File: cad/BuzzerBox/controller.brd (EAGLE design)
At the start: 100 x 100 mm, 137 parts, among them J2 RASPBERRYPI-40-PIN-GPIO_PTH_N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, Q1 BSS138, Q2 BSS138, Q3 BSS138, T1 BC849, T10 BC849, T2 BC849, T3 BC849, T4 BC849, T5 BC849, T6 BC849, T7 BC849, T8 BC849, T9 BC849, U1 ATMEGA328P-AU, Y1 16MHz

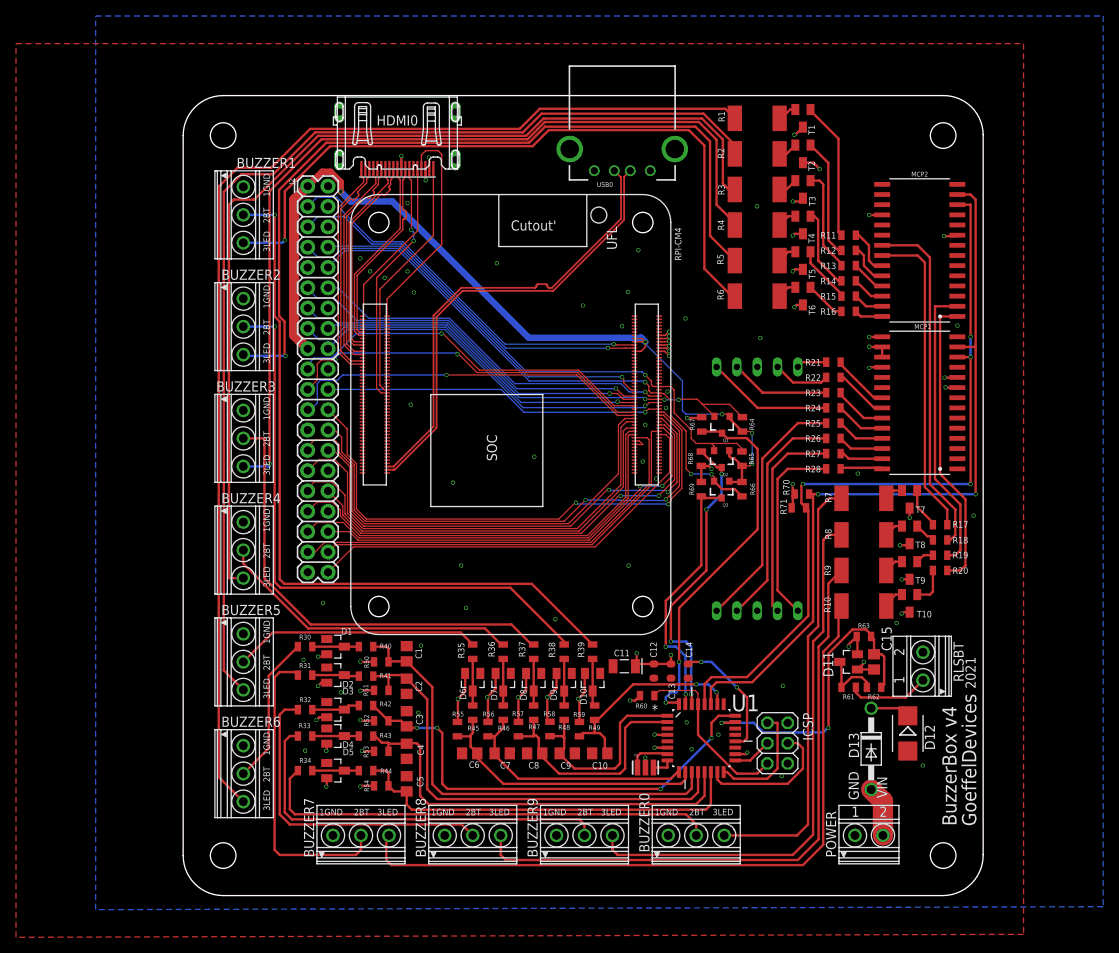
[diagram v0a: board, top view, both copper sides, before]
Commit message: Added combined header for buzzers
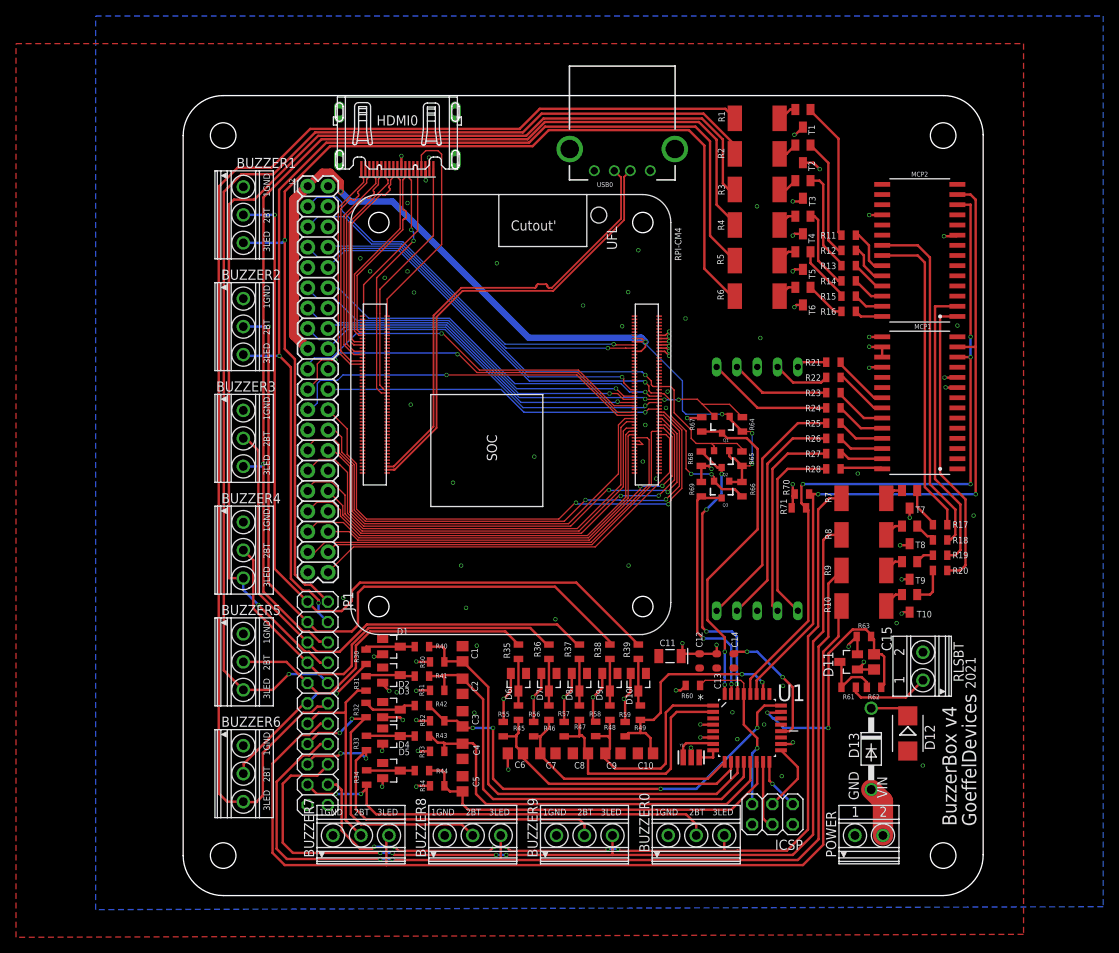
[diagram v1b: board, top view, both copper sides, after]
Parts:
- added JP1: (no value), pinhead:2X11
- moved ICSP 8.91 mm to (73.7, 10.2), turned to 180 degrees
- moved R34 7.74 mm to (22.9, 14.8), turned to 90 degrees
- moved R30 7.73 mm to (22.9, 29.8), turned to 90 degrees
- moved R33 7.72 mm to (22.9, 19.1), turned to 90 degrees
- moved R31 7.69 mm to (22.9, 26.5), turned to 90 degrees
- moved R32 7.62 mm to (22.9, 23.2), turned to 90 degrees
- moved D1 6.98 mm to (26.0, 31.1)
- moved D2 6.98 mm to (26.0, 27.6)
- moved D3 6.98 mm to (26.0, 23.2)
- moved D4 6.98 mm to (26.0, 19.9)
- moved D5 6.98 mm to (26.0, 15.6)
- moved R40 6.98 mm to (29.8, 31.1)
- moved R41 6.98 mm to (29.8, 27.4)
- moved R42 6.98 mm to (29.8, 23.7)
- moved R43 6.98 mm to (29.8, 19.9)
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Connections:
- removed net N$23: BUZZER6.2, R30.1
- removed net N$35: BUZZER7.2, R31.1
- removed net N$36: BUZZER3.2, R37.1
- removed net N$37: BUZZER1.2, R39.1
- removed net N$38: BUZZER2.2, R38.1
- removed net N$39: BUZZER9.2, R33.1
- removed net N$4: BUZZER8.2, R32.1
- removed net N$40: BUZZER0.2, R34.1
- removed net N$45: BUZZER5.2, R35.1
- removed net N$46: BUZZER4.2, R36.1
- new net BUZZ0: BUZZER0.2, JP1.19, R34.1
- new net BUZZ1: BUZZER1.2, JP1.1, R39.1
- new net BUZZ2: BUZZER2.2, JP1.3, R38.1
- new net BUZZ3: BUZZER3.2, JP1.5, R37.1
- new net BUZZ4: BUZZER4.2, JP1.7, R36.1
- new net BUZZ5: BUZZER5.2, JP1.9, R35.1
- new net BUZZ6: BUZZER6.2, JP1.11, R30.1
- new net BUZZ7: BUZZER7.2, JP1.13, R31.1
- new net BUZZ8: BUZZER8.2, JP1.15, R32.1
- new net BUZZ9: BUZZER9.2, JP1.17, R33.1
- net GND: now also JP1.21, JP1.22
- net LED0A2: now also JP1.12
- net LED0A3: now also JP1.10
- net LED0A4: now also JP1.8
- net LED0B0: now also JP1.14
- net LED0B1: now also JP1.16
- net LED1A0: now also JP1.18
- net LED1A1: now also JP1.20
- net LED1A5: now also JP1.6
- net LED1A6: now also JP1.4
- net LED1A7: now also JP1.2
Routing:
- net BUZZ1: track 0.00 -> 101.2 mm, vias 0 -> 1
- net N$37: track 92.2 -> 0.00 mm, vias 1 -> 0
- net BUZZ2: track 0.00 -> 88.7 mm, vias 0 -> 1
- net N$38: track 75.8 -> 0.00 mm, vias 1 -> 0
- net BUZZ3: track 0.00 -> 65.9 mm
- net LED1A1: track 54.4 -> 114.4 mm, vias 0 -> 6
- net N$40: track 58.2 -> 0.00 mm
- net N$36: track 57.2 -> 0.00 mm
- net LED1A0: track 68.1 -> 124.4 mm, vias 0 -> 4
- net BUZZ0: track 0.00 -> 54.7 mm, vias 0 -> 2
- net BUZZ4: track 0.00 -> 53.0 mm
- net N$39: track 50.3 -> 0.00 mm
- net BUZZ9: track 0.00 -> 48.0 mm, vias 0 -> 2
- net LED1A7: track 88.5 -> 136.3 mm
- net LED0B1: track 78.3 -> 124.0 mm, vias 0 -> 2
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
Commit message: Add Dc-Dc Circuit, for possible 12V supply
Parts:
- removed D13: 1N4002, diode:DO41-10
- added C16: 22uF, rcl:C0805
- added C17: 10uF, rcl:C0805
- added R29, R72: 0, SparkFun-Resistors:0805
- added U$5: GAPTECCLC78, gaptec:GAPTECLC78
- moved D12 8.34 mm to (85.3, 13.8), turned to 180 degrees
- moved RLSBT 1.02 mm to (92.4, 29.7)
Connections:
- removed net N$32: D13.A, POWER.2
- new net +12V: C17.1, D12.C, POWER.2, R29.2, R72.2, U$5.P$1
- net +5V: now also C16.2, R29.1, R72.1, U$5.P$3; no longer D12.C, D13.C
- net GND: now also C16.1, C17.2, U$5.P$2
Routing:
- net +12V: track 0.00 -> 37.7 mm
- net GND: track 16.6 -> 25.8 mm, vias 47 -> 49
- net +5V: track 111.3 -> 119.2 mm
- net N$32: track 6.35 -> 0.00 mm

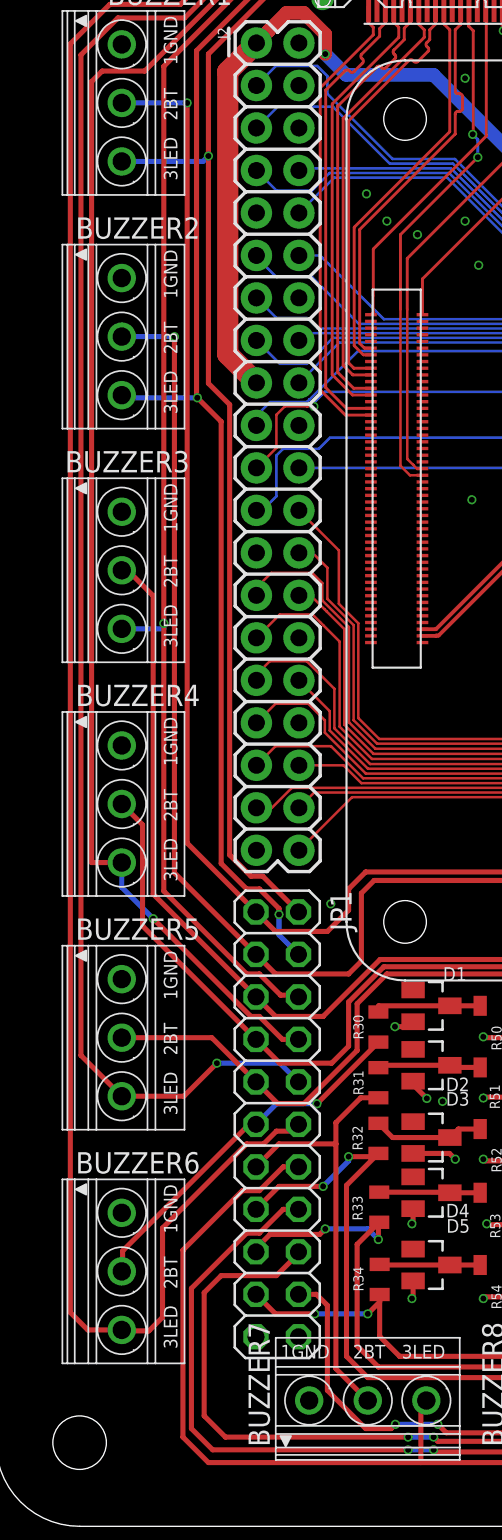
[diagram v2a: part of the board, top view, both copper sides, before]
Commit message: Reduce connector pitch to 2mm for XLR-Board-Connection
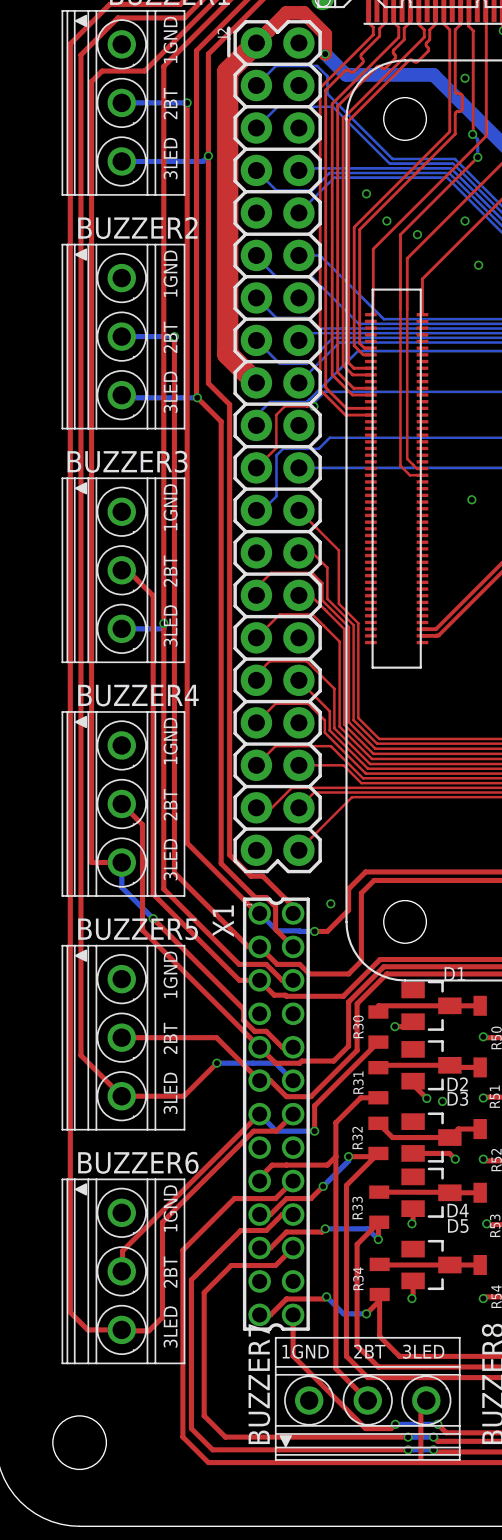
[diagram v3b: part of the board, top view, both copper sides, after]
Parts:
- removed JP1: (no value), pinhead:2X11
- added X1: 87758-2616, con-molex:87758-2616
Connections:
- net BUZZ0: now also X1.25; no longer JP1.19
- net BUZZ1: now also X1.1; no longer JP1.1
- net BUZZ2: now also X1.3; no longer JP1.3
- net BUZZ3: now also X1.5; no longer JP1.5
- net BUZZ4: now also X1.9; no longer JP1.7
- net BUZZ5: now also X1.11; no longer JP1.9
- net BUZZ6: now also X1.13; no longer JP1.11
- net BUZZ7: now also X1.17; no longer JP1.13
- net BUZZ8: now also X1.19; no longer JP1.15
- net BUZZ9: now also X1.21; no longer JP1.17
- net GND: now also X1.15, X1.16, X1.23, X1.24, X1.7, X1.8; no longer JP1.21, JP1.22
- net LED0A2: now also X1.14; no longer JP1.12
- net LED0A3: now also X1.12; no longer JP1.10
- net LED0A4: now also X1.10; no longer JP1.8
- net LED0B0: now also X1.18; no longer JP1.14
- net LED0B1: now also X1.20; no longer JP1.16
- net LED1A0: now also X1.22; no longer JP1.18
- net LED1A1: now also X1.26; no longer JP1.20
- net LED1A5: now also X1.6; no longer JP1.6
- net LED1A6: now also X1.4; no longer JP1.4
- net LED1A7: now also X1.2; no longer JP1.2
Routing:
- net BUZZ6: track 21.7 -> 23.4 mm
- net LED1A1: track 114.4 -> 112.6 mm
- net BUZZ3: track 65.9 -> 65.0 mm
- net LED1A5: track 135.9 -> 135.1 mm
- net LED0B0: track 125.5 -> 124.8 mm
- net LED1A6: track 135.7 -> 135.0 mm, vias 2 -> 1
- net BUZZ1: vias 1 -> 2

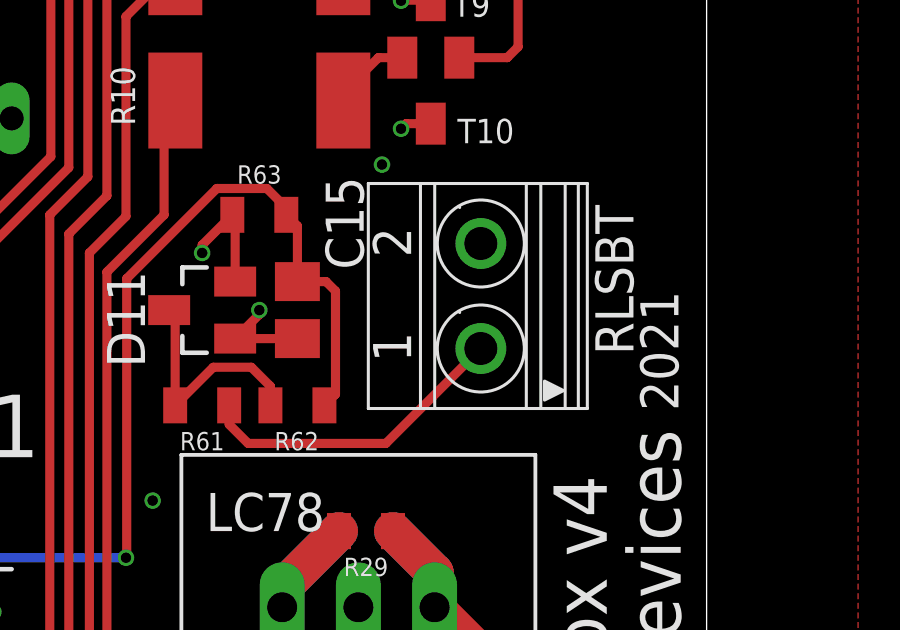
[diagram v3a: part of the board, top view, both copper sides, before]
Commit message: Reduce connector pitch to 2mm for Release button
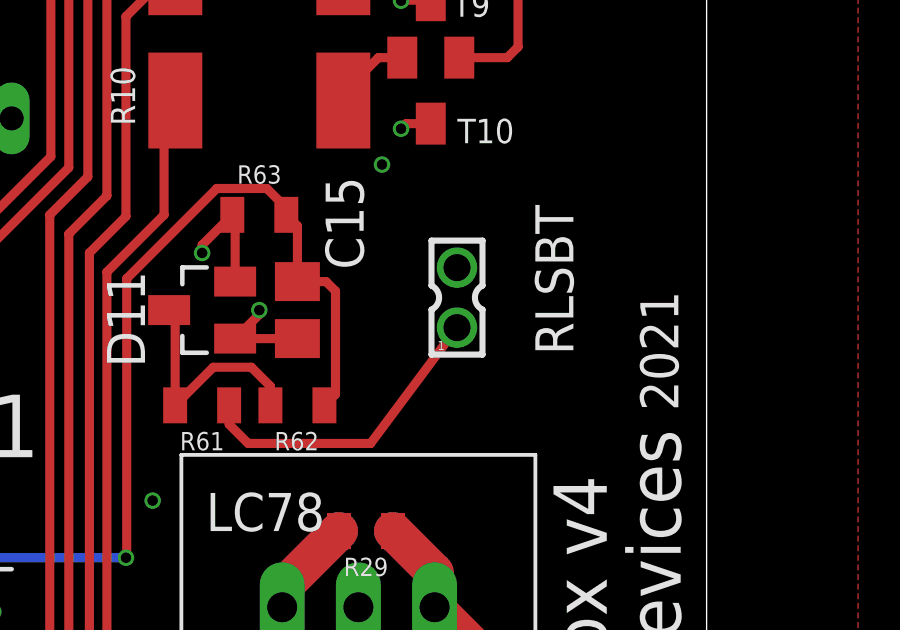
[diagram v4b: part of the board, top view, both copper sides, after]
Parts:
- RLSBT: value 1751248 -> 87758-0216; device con-phoenix-350:1751248 -> con-molex:87758-0216
- moved RLSBT 0.70 mm to (91.7, 29.6), turned to 0 degrees
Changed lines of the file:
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@@
 <attribute name="VALUE" x="95.885" y="52.07" size="0.4064" layer="27" font="vector" align="top-right"/>
 </element>
-<element name="RLSBT" library="con-phoenix-350" library_urn="urn:adsk.eagle:library:174" package="1751248" package3d_urn="urn:adsk.eagle:package:9395/1" value="1751248" x="92.3738" y="29.6798" smashed="yes" rot="R90">
-<attribute name="MF" value="" x="92.3738" y="29.6798" size="1.778" layer="27" rot="R90" display="off"/>
-<attribute name="MPN" value="" x="92.3738" y="29.6798" size="1.778" layer="27" rot="R90" display="off"/>
-<attribute name="NAME" x="96.2898" y="32.7113" size="1.27" layer="25" rot="R270"/>
-<attribute name="OC_FARNELL" value="unknown" x="92.3738" y="29.6798" size="1.778" layer="27" rot="R90" display="off"/>
-<attribute name="OC_NEWARK" value="unknown" x="92.3738" y="29.6798" size="1.778" layer="27" rot="R90" display="off"/>
-<attribute name="POPULARITY" value="24" x="92.3738" y="29.6798" size="1.778" layer="27" rot="R90" display="off"/>
-<attribute name="VALUE" x="88.2463" y="27.6273" size="1.27" layer="27" rot="R90"/>
+<element name="RLSBT" library="con-molex" library_urn="urn:adsk.eagle:library:165" package="87758-0216" package3d_urn="urn:adsk.eagle:package:8078894/1" value="87758-0216" x="91.6798" y="29.6262" smashed="yes">
+<attribute name="MF" value="MOLEX" x="91.6798" y="29.6262" size="1.778" layer="27" display="off"/>
+<attribute name="MPN" value="87758-0216" x="91.6798" y="29.6262" size="1.778" layer="27" display="off"/>
+<attribute name="NAME" x="94.2898" y="32.7113" size="1.27" layer="25" rot="R270"/>
+<attribute name="OC_FARNELL" value="unknown" x="91.6798" y="29.6262" size="1.778" layer="27" display="off"/>
+<attribute name="OC_NEWARK" value="94M1513" x="91.6798" y="29.6262" size="1.778" layer="27" display="off"/>
+<attribute name="POPULARITY" value="4" x="91.6798" y="29.6262" size="1.778" layer="27" display="off"/>
+<attribute name="VALUE" x="89.6273" y="33.7537" size="1.27" layer="27"/>
 </element>
 <element name="R71" library="SparkFun-Resistors" library_urn="urn:adsk.eagle:library:532" package="0805" package3d_urn="urn:adsk.eagle:package:39651/1" value=" " x="76.962" y="48.4632" smashed="yes" rot="R180">
@@
 <wire x1="84.72" y1="24.765" x2="84.085" y2="25.4" width="0.3048" layer="1"/>
 <wire x1="84.085" y1="26.035" x2="84.085" y2="25.4" width="0.3048" layer="1"/>
-<wire x1="89.309" y1="24.765" x2="92.4738" y2="27.9298" width="0.3048" layer="1"/>
-<wire x1="84.72" y1="24.765" x2="89.309" y2="24.765" width="0.3048" layer="1"/>
+<wire x1="88.800434375" y1="24.765" x2="91.6798" y2="28.6262" width="0.3048" layer="1"/>
+<wire x1="84.72" y1="24.765" x2="88.800434375" y2="24.765" width="0.3048" layer="1"/>
 </signal>
 <signal name="+12V">

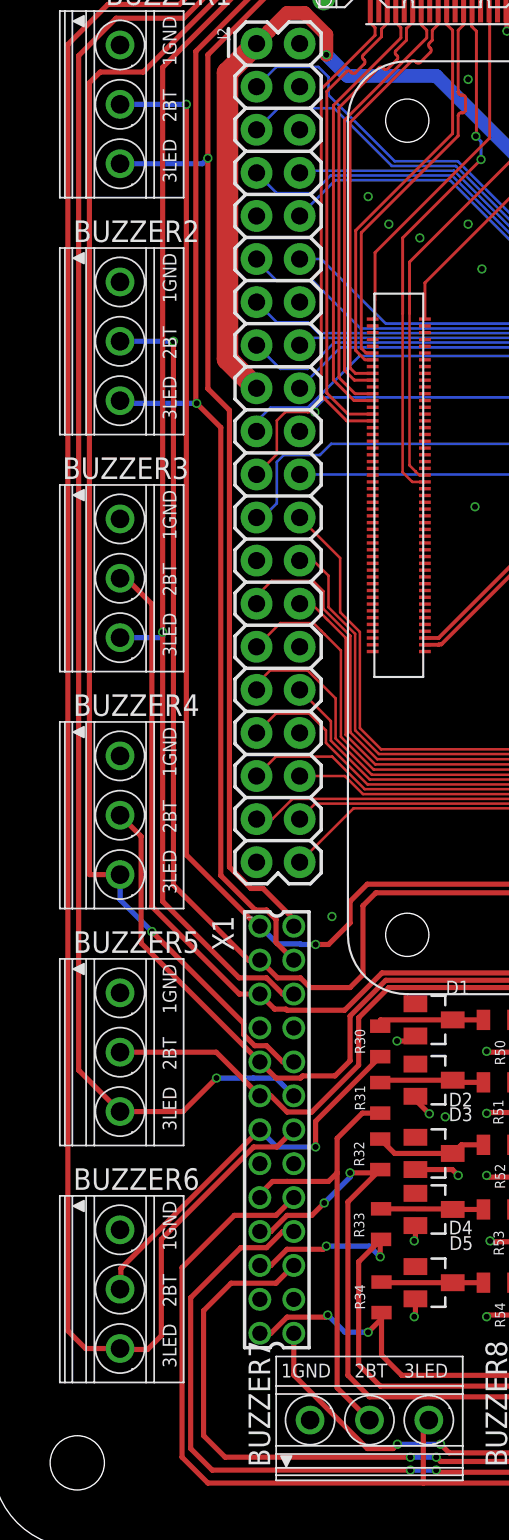
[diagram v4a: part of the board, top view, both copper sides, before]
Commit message: Move buzzer pcb connector away from GPIO Header
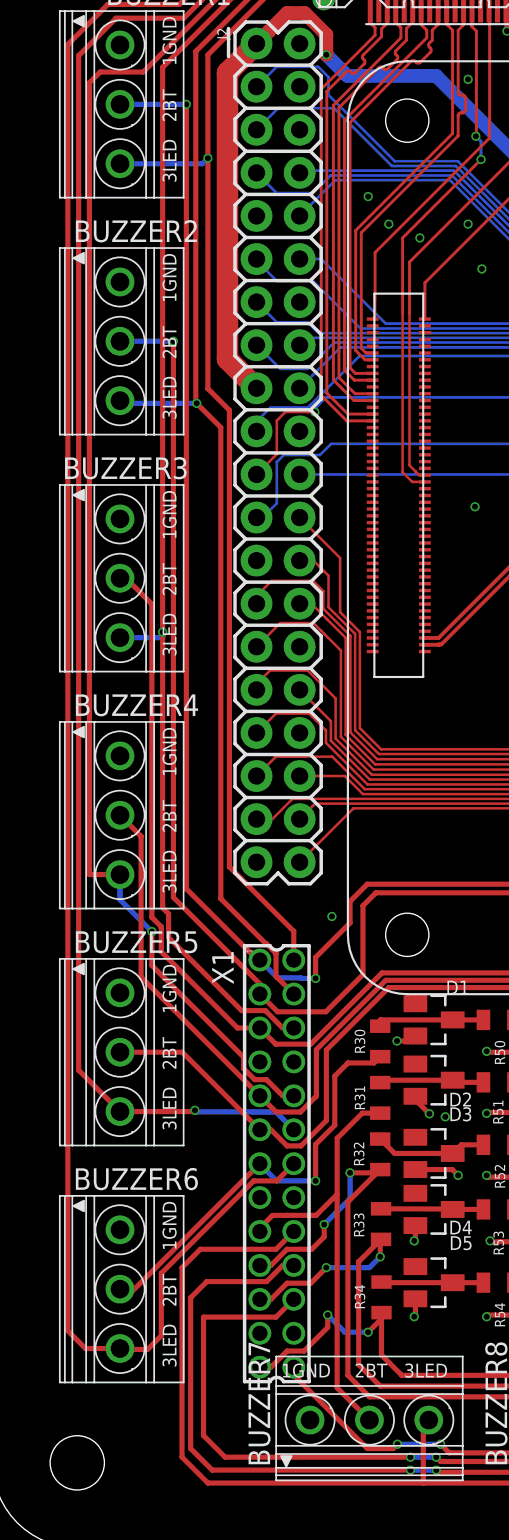
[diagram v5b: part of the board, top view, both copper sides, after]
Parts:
- moved X1 2.00 mm to (16.8, 22.6)
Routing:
- net BUZZ1: track 101.2 -> 104.8 mm
- net BUZZ3: track 65.0 -> 68.0 mm
- net BUZZ4: track 53.1 -> 56.0 mm
- net BUZZ5: track 41.2 -> 43.7 mm
- net LED1A1: track 112.6 -> 110.6 mm
- net LED0A4: track 139.2 -> 141.2 mm
- net LED0A2: track 167.3 -> 165.3 mm
- net BUZZ8: track 38.0 -> 40.0 mm
- net BUZZ2: track 88.7 -> 90.6 mm
- net LED1A5: track 135.1 -> 136.9 mm
- net BUZZ6: track 23.4 -> 25.2 mm
- net LED1A6: track 135.0 -> 136.7 mm
- net LED1A7: track 136.2 -> 137.8 mm
- net BUZZ0: track 54.8 -> 56.1 mm
- net LED1A0: track 124.1 -> 123.1 mm
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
